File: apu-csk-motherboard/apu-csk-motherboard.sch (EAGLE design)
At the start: 9 parts

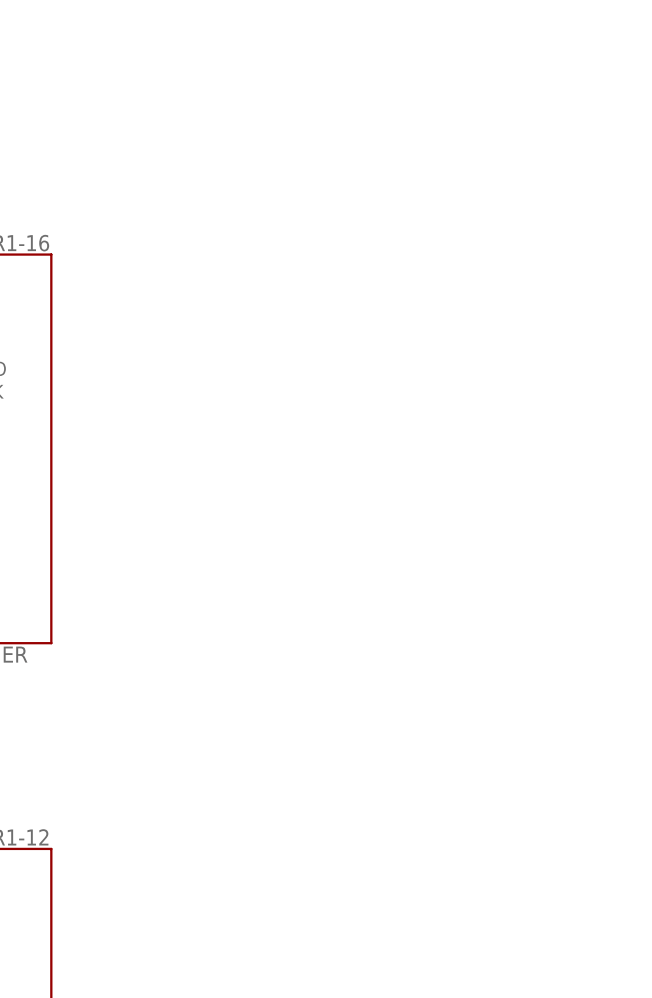
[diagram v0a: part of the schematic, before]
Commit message: added the sd card schematic to the library
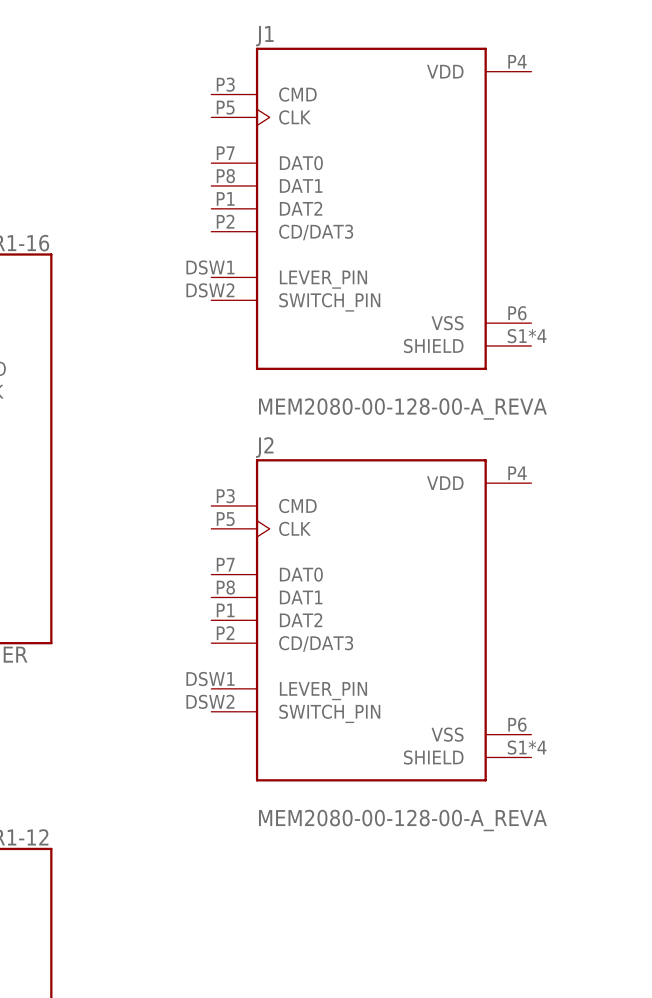
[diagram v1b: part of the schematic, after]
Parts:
- added J1, J2: MEM2080-00-128-00-A_REVA, MEM2080-00-128-00-A_REVA:MEM2080-00-128-00-A_REVA
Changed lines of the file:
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@@
 <part name="PL3" library="apu-csk-motherboard" deviceset="ICEWERX-PL3" device=""/>
 <part name="FRAME1" library="apu-csk-motherboard" deviceset="FRAME_LETTER_LANDSCAPE" device=""/>
+<part name="J1" library="MEM2080-00-128-00-A_REVA" deviceset="MEM2080-00-128-00-A_REVA" device=""/>
+<part name="J2" library="MEM2080-00-128-00-A_REVA" deviceset="MEM2080-00-128-00-A_REVA" device=""/>
 </parts>
 <sheets>
@@
 <attribute name="VALUE" x="177.8" y="113.03" size="1.778" layer="96" align="center"/>
 </instance>
+<instance part="J1" gate="G$1" x="220.98" y="162.56" smashed="yes">
+<attribute name="NAME" x="208.28" y="181.102" size="1.778" layer="95"/>
+<attribute name="VALUE" x="208.28" y="139.7" size="1.778" layer="96"/>
+</instance>
+<instance part="J2" gate="G$1" x="220.98" y="116.84" smashed="yes">
+<attribute name="NAME" x="208.28" y="135.382" size="1.778" layer="95"/>
+<attribute name="VALUE" x="208.28" y="93.98" size="1.778" layer="96"/>
+</instance>
 </instances>

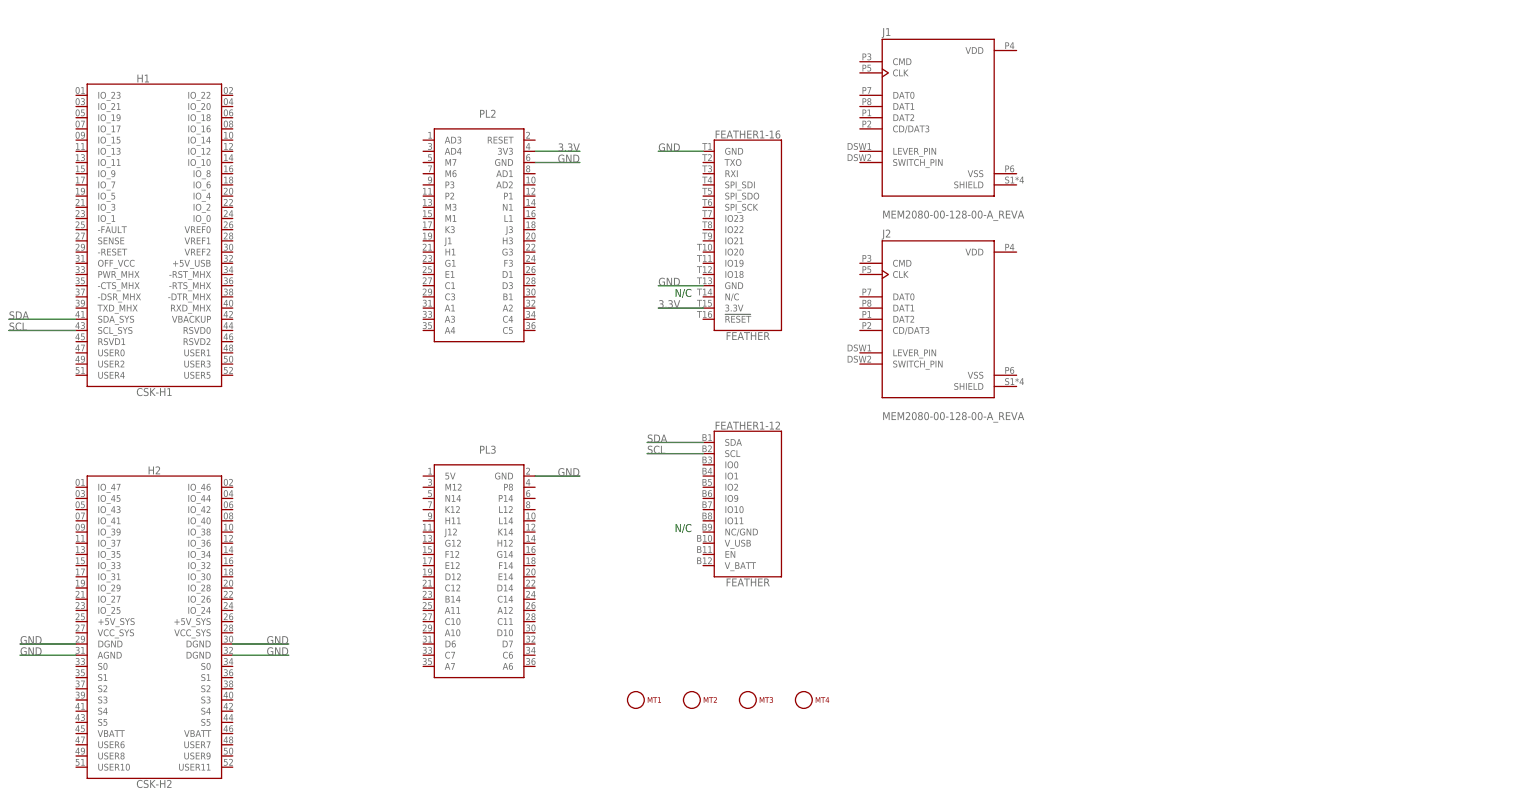
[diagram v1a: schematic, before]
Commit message: Started Connecting the SD Card to the MicroController
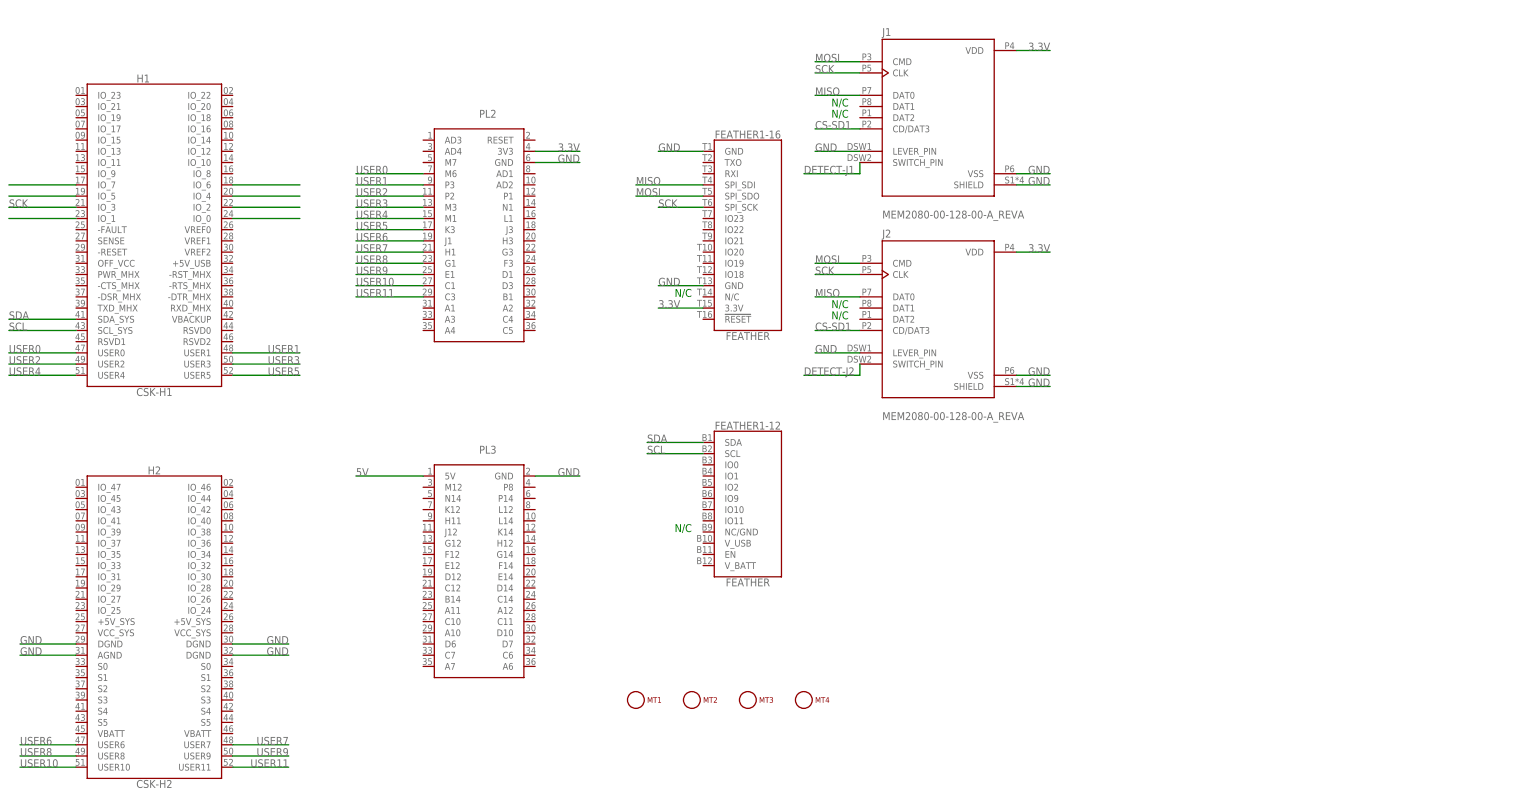
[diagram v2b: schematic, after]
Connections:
- new net 5V: PL3.5V@1
- new net CS-SD1: J1.CD/DAT3, J2.CD/DAT3
- new net DETECT-J1: J1.SWITCH_PIN
- new net DETECT-J2: J2.SWITCH_PIN
- new net MISO: FEATHER1-16.SPI_SDI@T4, J1.DAT0, J2.DAT0
- new net MOSI: FEATHER1-16.SPI_SDO@T5, J1.CMD, J2.CMD
- new net N$1: H1.IO_0@24
- new net N$2: H1.IO_2@22
- new net N$3: H1.IO_4@20
- new net N$4: H1.IO_6@18
- new net N$5: H1.IO_1@23
- new net N$7: H1.IO_5@19
- new net N$8: H1.IO_7@17
- new net SCK: FEATHER1-16.SPI_SCK@T6, H1.IO_3@21, J1.CLK, J2.CLK
- new net USER0: H1.USER0@47, PL2.M6@7
- new net USER1: H1.USER1@48, PL2.P3@9
- new net USER10: H2.USER10@51, PL2.C1@27
- new net USER11: H2.USER11@52, PL2.C3@29
- new net USER2: H1.USER2@49, PL2.P2@11
- new net USER3: H1.USER3@50, PL2.M3@13
- new net USER4: H1.USER4@51, PL2.M1@15
- new net USER5: H1.USER5@52, PL2.K3@17
- new net USER6: H2.USER6@47, PL2.J1@19
- new net USER7: H2.USER7@48, PL2.H1@21
- new net USER8: H2.USER8@49, PL2.G1@23
- new net USER9: H2.USER9@50, PL2.E1@25
- net 3.3V: now also J1.VDD, J2.VDD
- net GND: now also J1.LEVER_PIN, J1.SHIELD, J1.VSS, J2.LEVER_PIN, J2.SHIELD, J2.VSS

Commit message: Proper SD Card
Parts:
- removed J1, J2: MEM2080-00-128-00-A_REVA, MEM2080-00-128-00-A_REVA:MEM2080-00-128-00-A_REVA
- added SD-1, SD-2: 503182-1852, 503182-1852:503182-1852
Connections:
- removed net CS-SD1: J1.CD/DAT3, J2.CD/DAT3
- removed net DETECT-J1: J1.SWITCH_PIN
- removed net DETECT-J2: J2.SWITCH_PIN
- removed net MISO: FEATHER1-16.SPI_SDI@T4, J1.DAT0, J2.DAT0
- removed net MOSI: FEATHER1-16.SPI_SDO@T5, J1.CMD, J2.CMD
- new net CIPO: FEATHER1-16.SPI_SDI@T4, SD-1.DAT0, SD-2.DAT0
- new net COPI: FEATHER1-16.SPI_SDO@T5, SD-1.CMD, SD-2.CMD
- new net CS-1: FEATHER1-16.IO18@T12, SD-1.CD/DAT3
- new net CS-2: FEATHER1-16.IO19@T11, SD-2.CD/DAT3
- new net DETECT-1: SD-1.DETECT
- new net DETECT-2: SD-2.DETECT
- net 3.3V: now also SD-1.VDD, SD-2.VDD; no longer J1.VDD, J2.VDD
- net GND: now also SD-1.SHIELD, SD-1.SWITCH, SD-1.VSS, SD-2.SHIELD, SD-2.SWITCH, SD-2.VSS; no longer J1.LEVER_PIN, J1.SHIELD, J1.VSS, J2.LEVER_PIN, J2.SHIELD, J2.VSS
- net SCK: now also SD-1.CLK, SD-2.CLK; no longer J1.CLK, J2.CLK

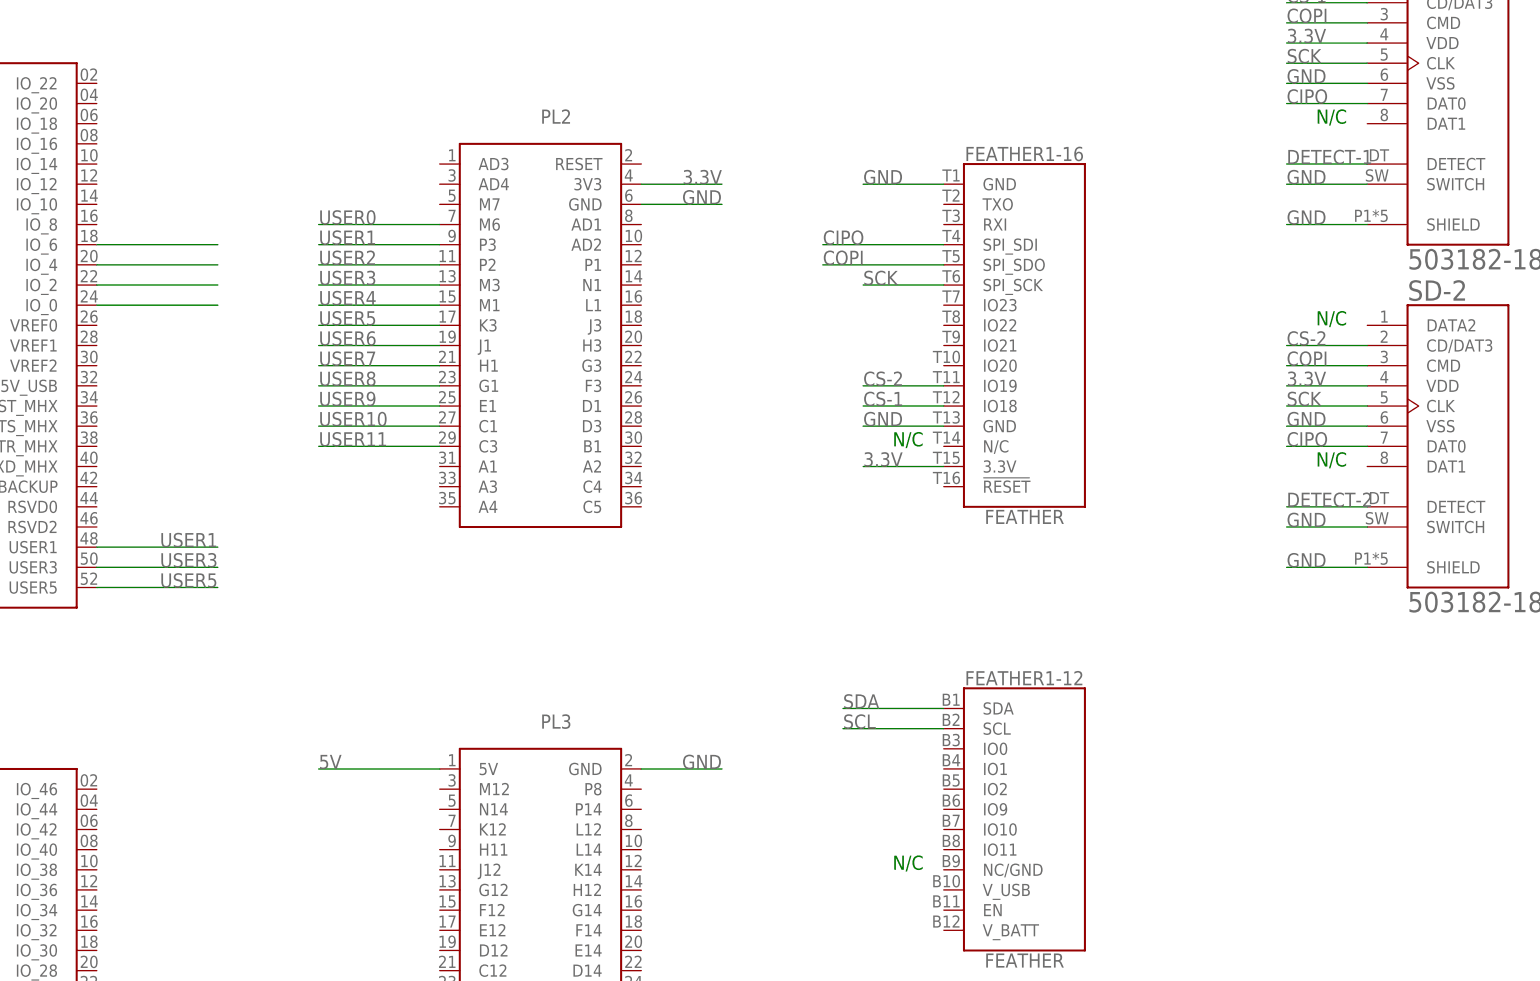
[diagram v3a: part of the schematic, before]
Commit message: Corrected the Detect and Swith on the SD Card
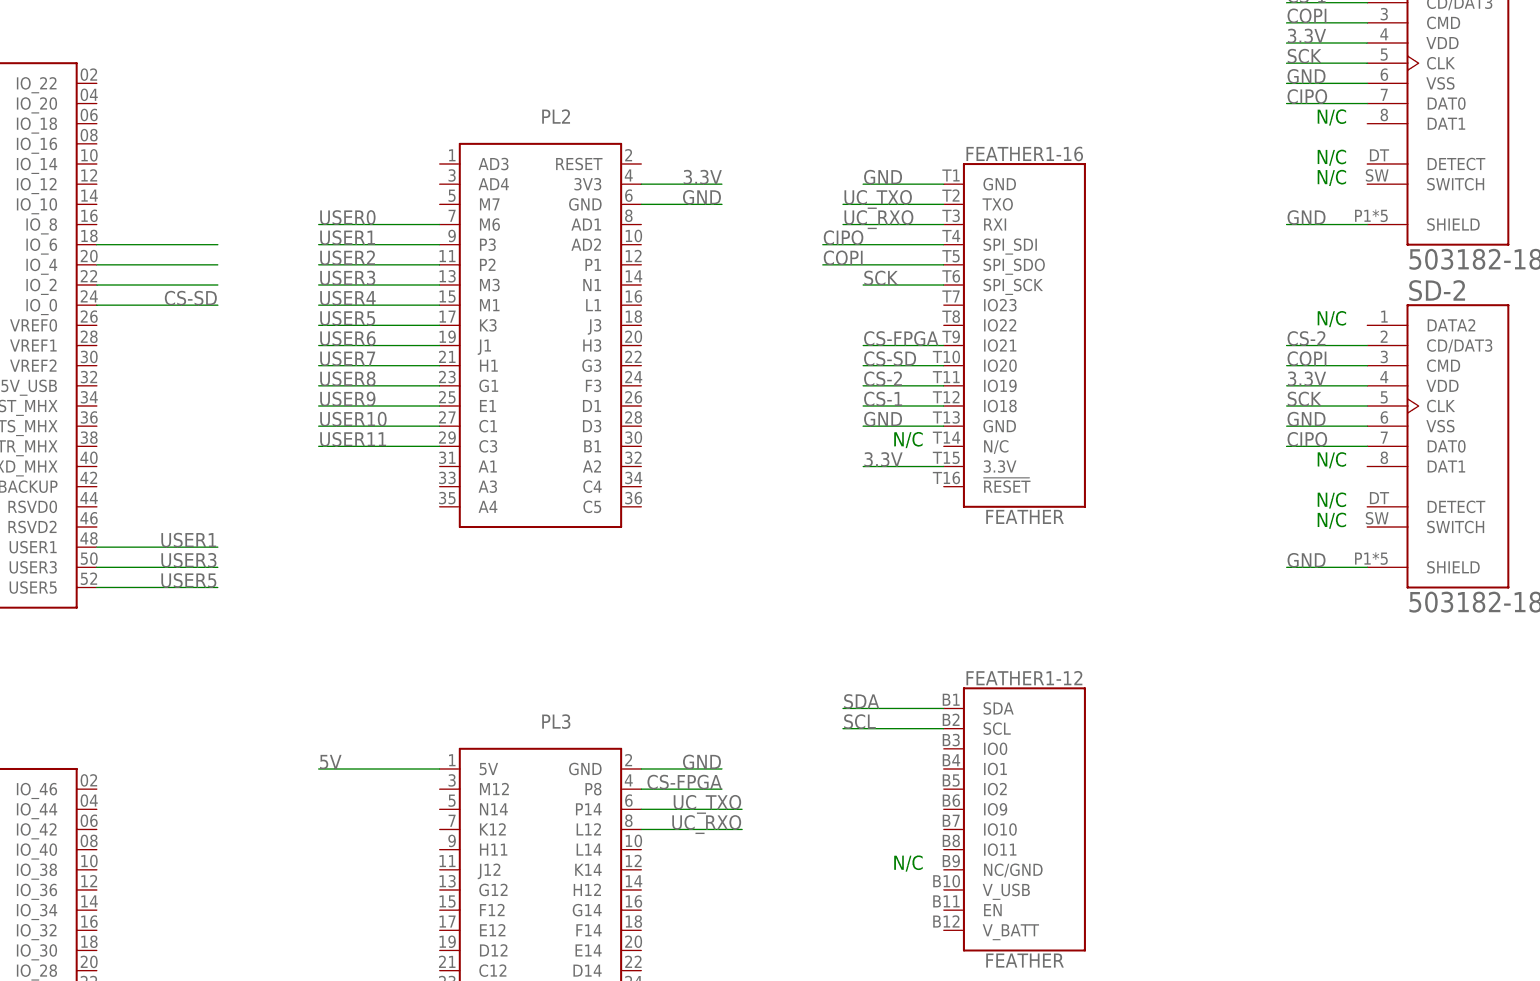
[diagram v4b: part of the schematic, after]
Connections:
- removed net DETECT-1: SD-1.DETECT
- removed net DETECT-2: SD-2.DETECT
- removed net N$1: H1.IO_0@24
- new net CS-FPGA: FEATHER1-16.IO21@T9, PL3.P8@4
- new net CS-SD: FEATHER1-16.IO20@T10, H1.IO_0@24
- new net UC_RXO: FEATHER1-16.RXI@T3, PL3.L12@8
- new net UC_TXO: FEATHER1-16.TXO@T2, PL3.P14@6
- net GND: no longer SD-1.SWITCH, SD-2.SWITCH
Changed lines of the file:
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@@
 <text x="218.44" y="162.56" size="1.778" layer="91" rot="MR0">N/C</text>
 <text x="218.44" y="180.34" size="1.778" layer="91" rot="MR0">N/C</text>
+<text x="218.44" y="157.48" size="1.778" layer="91" rot="MR0">N/C</text>
+<text x="218.44" y="154.94" size="1.778" layer="91" rot="MR0">N/C</text>
+<text x="218.44" y="114.3" size="1.778" layer="91" rot="MR0">N/C</text>
+<text x="218.44" y="111.76" size="1.778" layer="91" rot="MR0">N/C</text>
 </plain>
 <instances>
@@
 </segment>
 <segment>
-<pinref part="SD-2" gate="G$1" pin="SWITCH"/>
-<wire x1="210.82" y1="111.76" x2="220.98" y2="111.76" width="0.1524" layer="91"/>
-<label x="210.82" y="111.76" size="1.778" layer="95"/>
-</segment>
-<segment>
 <pinref part="SD-1" gate="G$1" pin="SHIELD"/>
 <wire x1="210.82" y1="149.86" x2="220.98" y2="149.86" width="0.1524" layer="91"/>
@@
 </segment>
 <segment>
-<pinref part="SD-1" gate="G$1" pin="SWITCH"/>
-<wire x1="210.82" y1="154.94" x2="220.98" y2="154.94" width="0.1524" layer="91"/>
-<label x="210.82" y="154.94" size="1.778" layer="95"/>
-</segment>
-<segment>
 <pinref part="SD-1" gate="G$1" pin="VSS"/>
 <wire x1="210.82" y1="167.64" x2="220.98" y2="167.64" width="0.1524" layer="91"/>
@@
 </segment>
 </net>
-<net name="N$1" class="0">
-<segment>
-<pinref part="H1" gate="G$1" pin="IO_0@24"/>
-<wire x1="76.2" y1="139.7" x2="60.96" y2="139.7" width="0.1524" layer="91"/>
-</segment>
-</net>
 <net name="N$2" class="0">
 <segment>
@@
 <pinref part="H1" gate="G$1" pin="IO_7@17"/>
 <wire x1="10.16" y1="147.32" x2="25.4" y2="147.32" width="0.1524" layer="91"/>
-</segment>
-</net>
-<net name="DETECT-1" class="0">
-<segment>
-<pinref part="SD-1" gate="G$1" pin="DETECT"/>
-<wire x1="210.82" y1="157.48" x2="220.98" y2="157.48" width="0.1524" layer="91"/>
-<label x="210.82" y="157.48" size="1.778" layer="95"/>
 </segment>
 </net>
@@
 </segment>
 </net>
-<net name="DETECT-2" class="0">
-<segment>
-<pinref part="SD-2" gate="G$1" pin="DETECT"/>
-<wire x1="210.82" y1="114.3" x2="220.98" y2="114.3" width="0.1524" layer="91"/>
-<label x="210.82" y="114.3" size="1.778" layer="95"/>
-</segment>
-</net>
+<net name="CS-SD" class="0">
+<segment>
+<pinref part="FEATHER1" gate="-16" pin="IO20@T10"/>
+<wire x1="157.48" y1="132.08" x2="167.64" y2="132.08" width="0.1524" layer="91"/>
+<label x="157.48" y="132.08" size="1.778" layer="95"/>
+</segment>
+<segment>
+<pinref part="H1" gate="G$1" pin="IO_0@24"/>
+<wire x1="76.2" y1="139.7" x2="60.96" y2="139.7" width="0.1524" layer="91"/>
+<label x="76.2" y="139.7" size="1.778" layer="95" rot="MR0"/>
+</segment>
+</net>
+<net name="UC_RXO" class="0">
+<segment>
+<pinref part="FEATHER1" gate="-16" pin="RXI@T3"/>
+<wire x1="154.94" y1="149.86" x2="167.64" y2="149.86" width="0.1524" layer="91"/>
+<label x="154.94" y="149.86" size="1.778" layer="95"/>
+</segment>
+<segment>
+<pinref part="PL3" gate="G$1" pin="L12@8"/>
+<wire x1="129.54" y1="73.66" x2="142.24" y2="73.66" width="0.1524" layer="91"/>
+<label x="142.24" y="73.66" size="1.778" layer="95" rot="MR0"/>
+</segment>
+</net>
+<net name="UC_TXO" class="0">
+<segment>
+<pinref part="FEATHER1" gate="-16" pin="TXO@T2"/>
+<wire x1="154.94" y1="152.4" x2="167.64" y2="152.4" width="0.1524" layer="91"/>
+<label x="154.94" y="152.4" size="1.778" layer="95"/>
+</segment>
+<segment>
+<pinref part="PL3" gate="G$1" pin="P14@6"/>
+<wire x1="142.24" y1="76.2" x2="129.54" y2="76.2" width="0.1524" layer="91"/>
+<label x="142.24" y="76.2" size="1.778" layer="95" rot="MR0"/>
+</segment>
+</net>
+<net name="CS-FPGA" class="0">
+<segment>
+<pinref part="FEATHER1" gate="-16" pin="IO21@T9"/>
+<wire x1="157.48" y1="134.62" x2="167.64" y2="134.62" width="0.1524" layer="91"/>
+<label x="157.48" y="134.62" size="1.778" layer="95"/>
+</segment>
+<segment>
+<pinref part="PL3" gate="G$1" pin="P8@4"/>
+<wire x1="129.54" y1="78.74" x2="139.7" y2="78.74" width="0.1524" layer="91"/>
+<label x="139.7" y="78.74" size="1.778" layer="95" rot="MR0"/>
+</segment>
+</net>
